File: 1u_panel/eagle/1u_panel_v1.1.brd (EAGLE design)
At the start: 82 x 100 mm, 59 parts, among them Q3 MMBT3904, U2 TCAN330, U3 LM3671MF-3.3, U4 ZSPM4521, U5 LTC2990, U6 STM32F042K6, X1 16MHZ-2.5x2mm

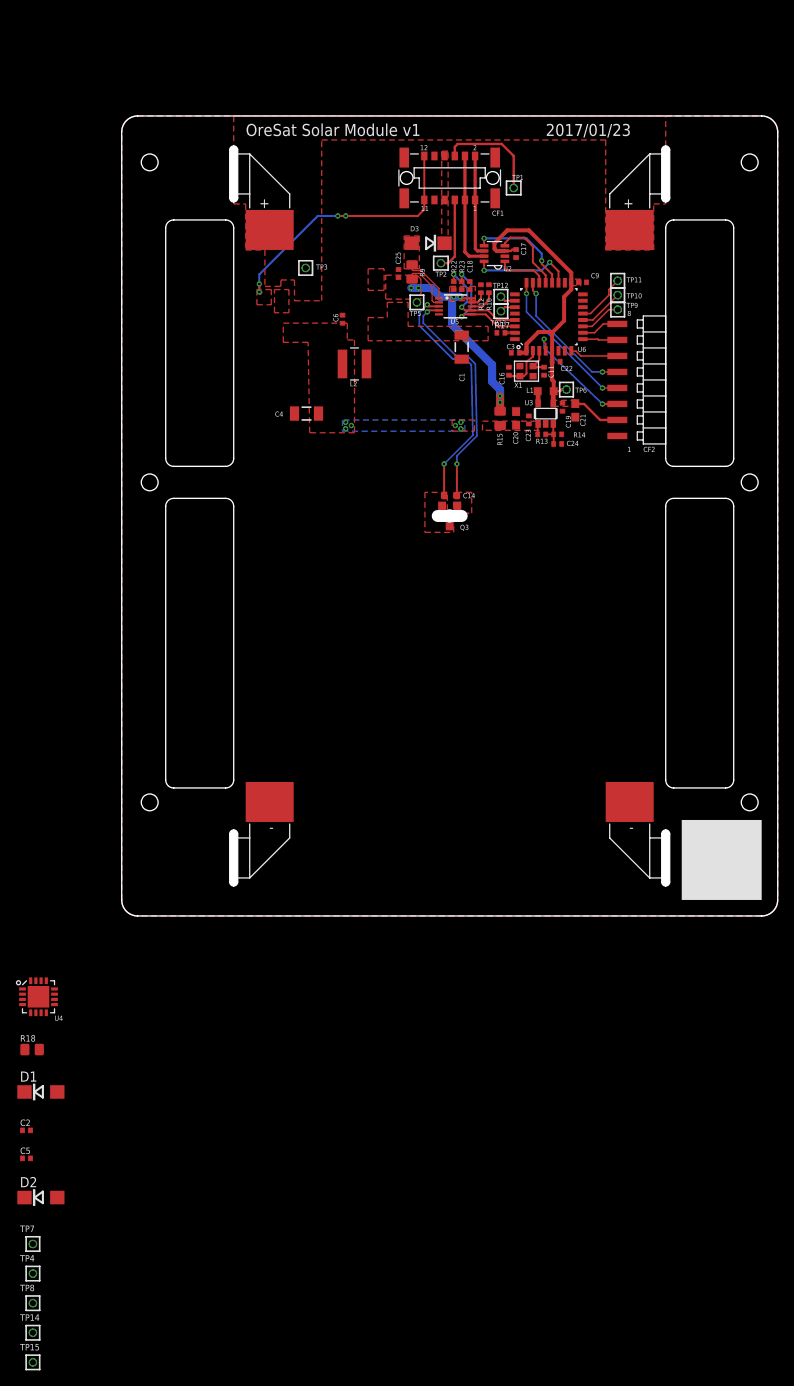
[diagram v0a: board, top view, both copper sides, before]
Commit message: First version of the 1.1 solar panel. Keeping 1.0 for future reference.
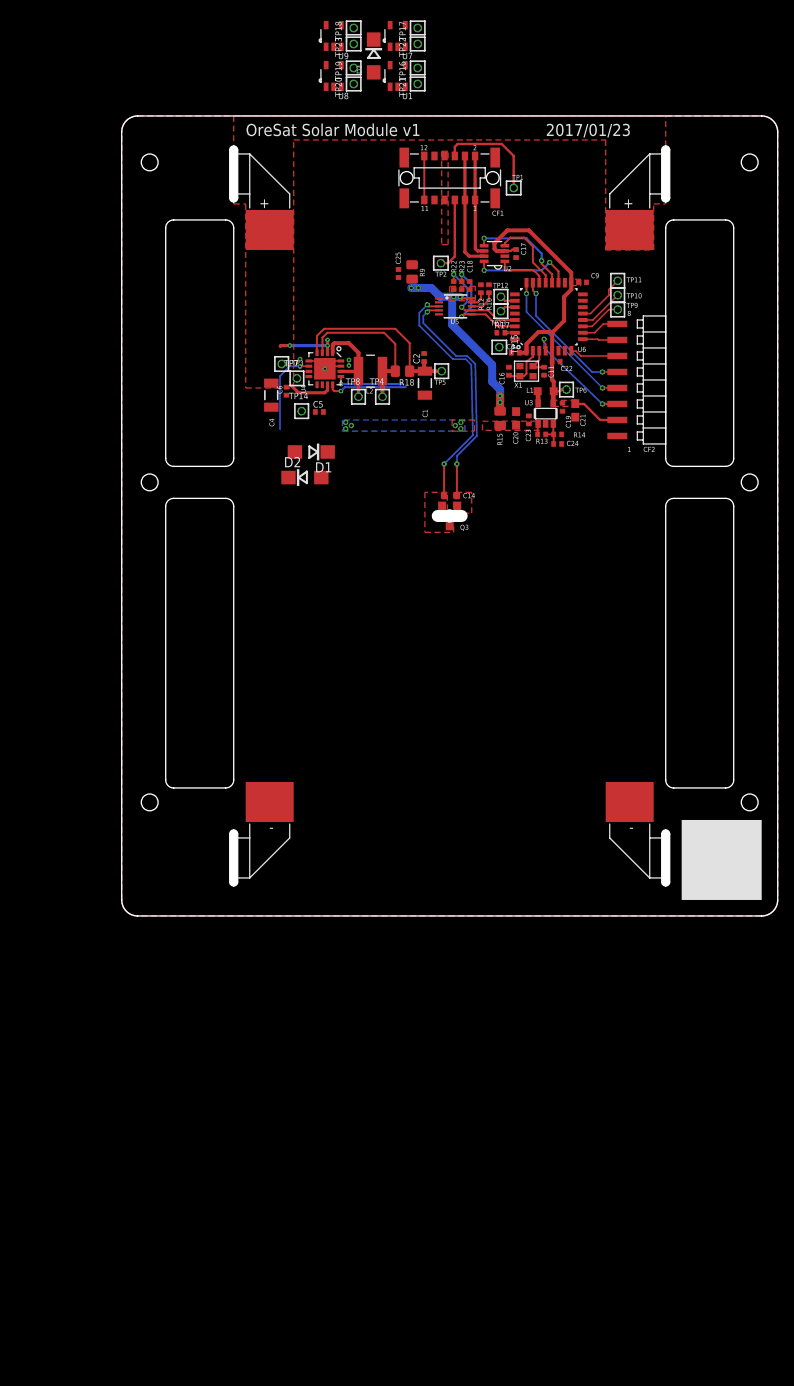
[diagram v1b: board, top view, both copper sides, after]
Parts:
- added TP16, TP17, TP18, TP19, TP20, TP21, TP22, TP23: TEST-POINT, Tova:2MM-TEST-POINT
- added U1, U7, U8, U9: LTC4411, ltc4411:SOT23-5-B
- D3: value STPS1L40AY -> DNP/STPS1L40AY
- moved TP15 139.7 mm to (47.2, 71.1), turned to 270 degrees
- moved TP8 120.4 mm to (29.6, 64.9)
- moved TP14 120.0 mm to (22.5, 63.1)
- moved TP4 118.0 mm to (32.6, 64.9)
- moved TP7 113.1 mm to (21.9, 67.2)
- moved C2 108.6 mm to (37.8, 69.8), turned to 90 degrees
- moved C5 100.2 mm to (24.7, 63.0)
- moved R18 96.6 mm to (35.1, 68.1), turned to 180 degrees
- moved D2 95.9 mm to (22.9, 54.8)
- moved D1 86.8 mm to (23.7, 58.0), turned to 180 degrees
- moved U4 86.3 mm to (25.4, 68.4), turned to 270 degrees
- moved D3 24.4 mm to (31.5, 107.5), turned to 270 degrees
- moved TP3 12.4 mm to (20.0, 69.0)
- moved C6 11.4 mm to (20.6, 65.6)
- moved TP5 9.14 mm to (40.0, 68.1)
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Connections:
- net N$13 renamed ZSPM_EN
- new net N$12: U1.5, U7.1
- new net N$15: U8.5, U9.1
- new net N$16: TP16.1, U1.4
- new net N$17: TP23.1, U9.3
- new net N$18: TP17.1, U7.4
- new net N$19: TP18.1, U9.4
- new net N$20: TP19.1, U8.4
- new net N$21: TP22.1, U7.3
- new net N$22: TP21.1, U1.3
- new net N$23: TP20.1, U8.3
- net GND: now also U1.2, U7.2, U8.2, U9.2
- net VPV: now also U7.5, U9.5
- net VSOLAR: now also U1.1, U8.1
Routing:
- net !SHDN-ORESAT: track 35.4 -> 5.50 mm, vias 4 -> 0
- net N$5: track 0.00 -> 20.0 mm
- net MPPT-OUT: track 32.0 -> 49.0 mm
- net SOLAR-IN: track 0.00 -> 13.3 mm, vias 0 -> 3
- net N$2: track 0.00 -> 12.7 mm
- net ZSPM_EN: track 0.00 -> 10.8 mm, vias 0 -> 1
- net SCL: track 13.3 -> 23.3 mm, vias 2 -> 3
- net SDA: track 14.6 -> 23.3 mm, vias 2 -> 3
- net GND: track 0.00 -> 6.94 mm, vias 0 -> 4
- net VSOLAR: track 6.18 -> 0.00 mm
- removed copper zone on layer 1, net !SHDN-ORESAT
- removed copper zone on layer 1, net N6
- removed copper zone on layer 1, net VCTRL
- removed copper zone on layer 1, net VOUT
- removed copper zone on layer 1, net VSOLAR
